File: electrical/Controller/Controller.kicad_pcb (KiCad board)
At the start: 2 copper layers, 30 x 42 mm, 33 parts, among them J1 USB4105-GF-A, J2 SWD_10, J3 TC2030-NL, U1 LP5912-3.3DRV, U2 USBLC6-2P6, U3 STM32L072CBTx, U4 ABPMRRV001PD2A3

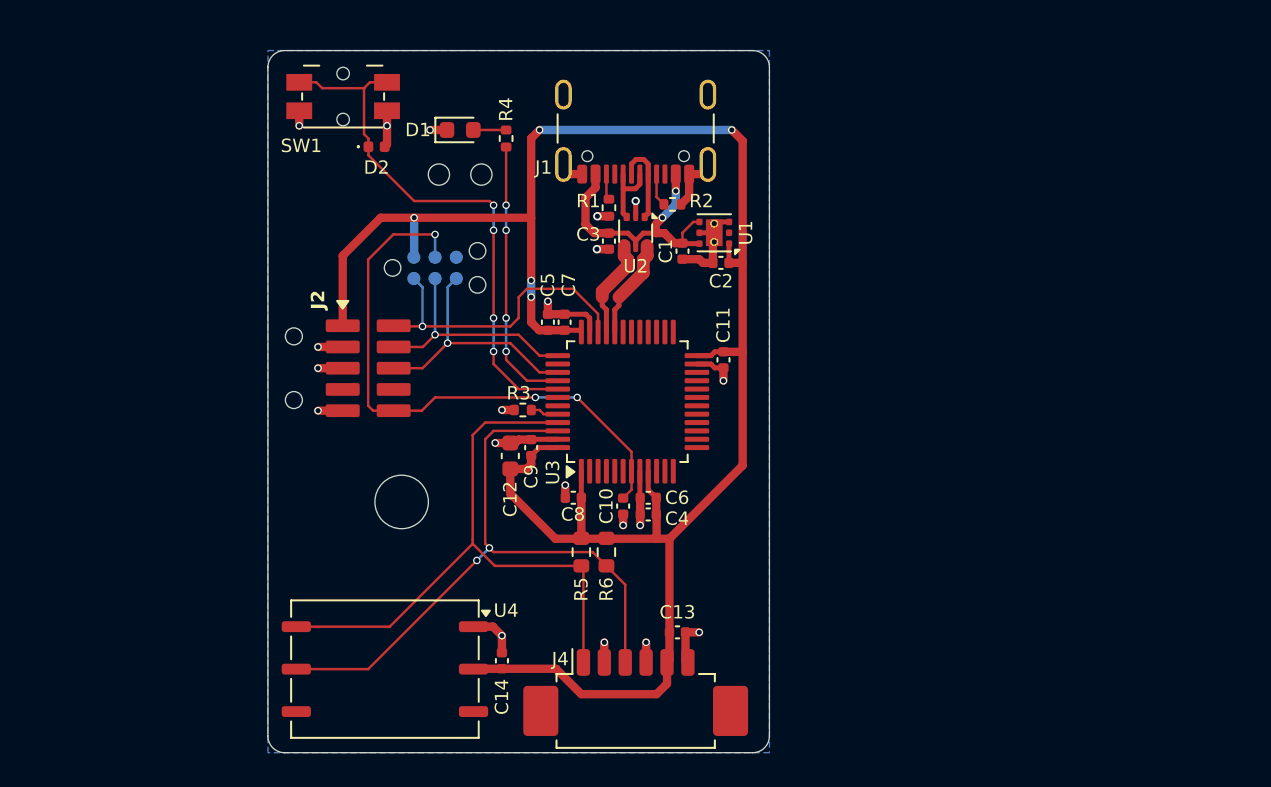
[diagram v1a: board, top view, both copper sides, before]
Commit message: Use wide layout for controller PCB
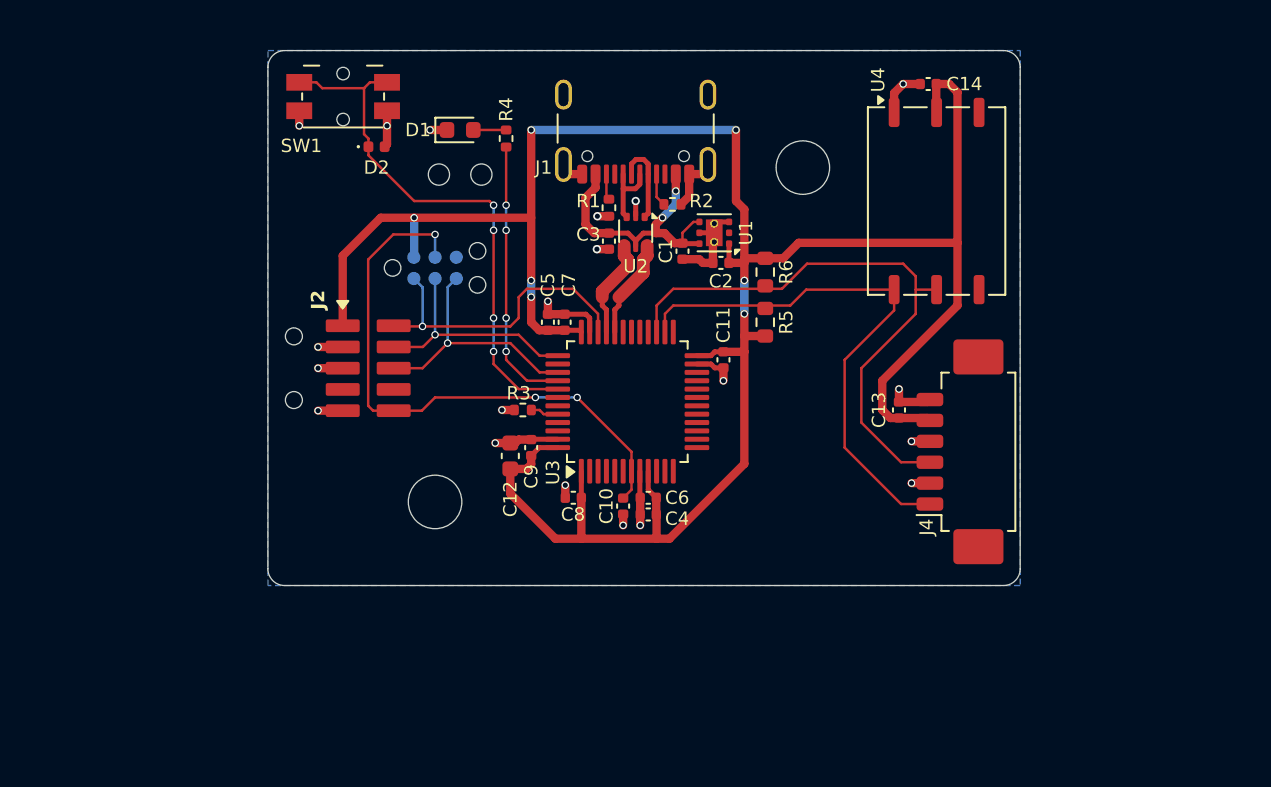
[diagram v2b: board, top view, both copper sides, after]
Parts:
- added H3: MountingHole, MountingHole:MountingHole_3.2mm_M3, F.Cu at (140.0, 97.0)
- moved U4 43.3 mm to (170.0, 79.0), turned to 0 degrees
- moved C14 42.9 mm to (169.5, 72.0), turned to 180 degrees
- moved H2 31.2 mm to (162.0, 77.0)
- moved J4 25.0 mm to (172.0, 94.0), turned to 90 degrees
- moved R6 19.3 mm to (159.8, 83.2)
- moved C13 18.8 mm to (167.8, 91.5), turned to 90 degrees
- moved R5 17.6 mm to (159.8, 86.2), turned to 90 degrees
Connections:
- U3 pad 26: unconnected-(U3-PB13-Pad26) -> /I2C_SCL
- U3 pad 27: unconnected-(U3-PB14-Pad27) -> /I2C_SDA
- U3 pad 45: /I2C_SCL -> unconnected-(U3-PB8-Pad45)
- U3 pad 46: /I2C_SDA -> unconnected-(U3-PB9-Pad46)
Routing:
- net +3.3V: track 121.8 -> 142.9 mm, vias 5 -> 7
- net /I2C_SCL: track 37.4 -> 32.6 mm
- net /I2C_SDA: track 39.4 -> 34.9 mm, vias 2 -> 0
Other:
- board size 30 x 42 mm -> 45 x 32 mm

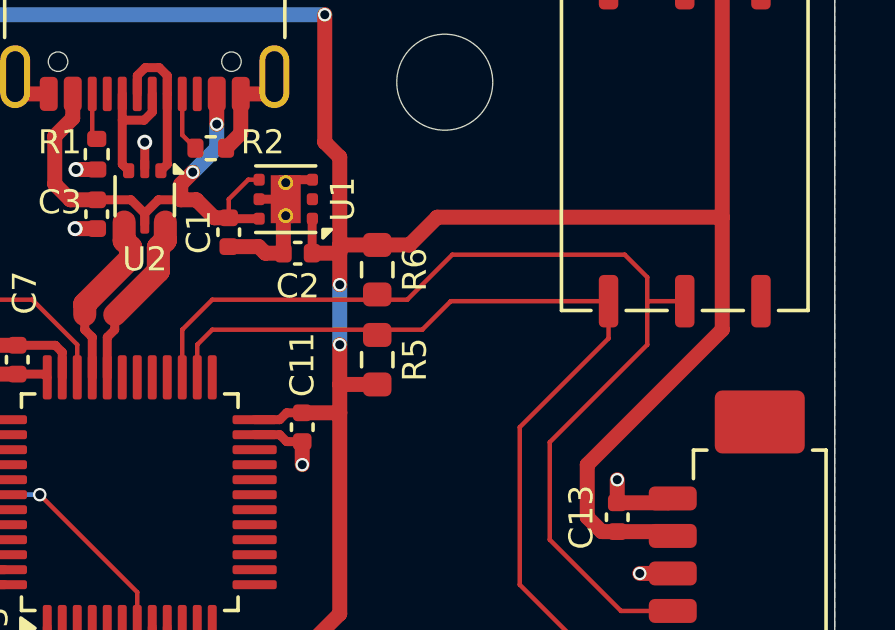
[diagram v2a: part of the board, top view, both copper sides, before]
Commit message: Use 0402 resistors for i2c pull-ups
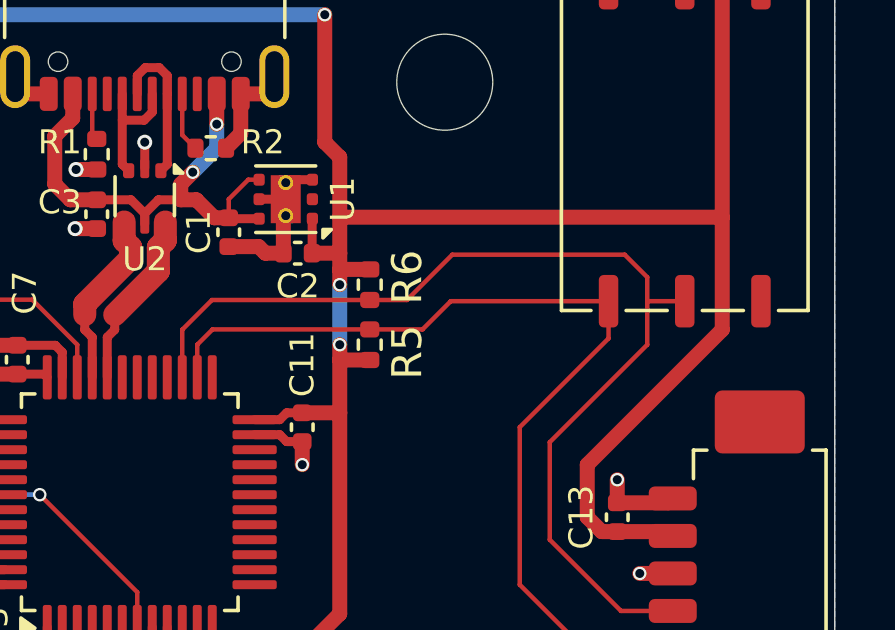
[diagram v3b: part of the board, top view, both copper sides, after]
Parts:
- R5, R6: footprint Resistor_SMD:R_0603_1608Metric -> Resistor_SMD:R_0402_1005Metric
- moved R5 0.56 mm to (159.5, 85.8)
- moved R6 0.56 mm to (159.5, 83.8)
- renumbered H2 to H1, H3 to H2, H1 to H3

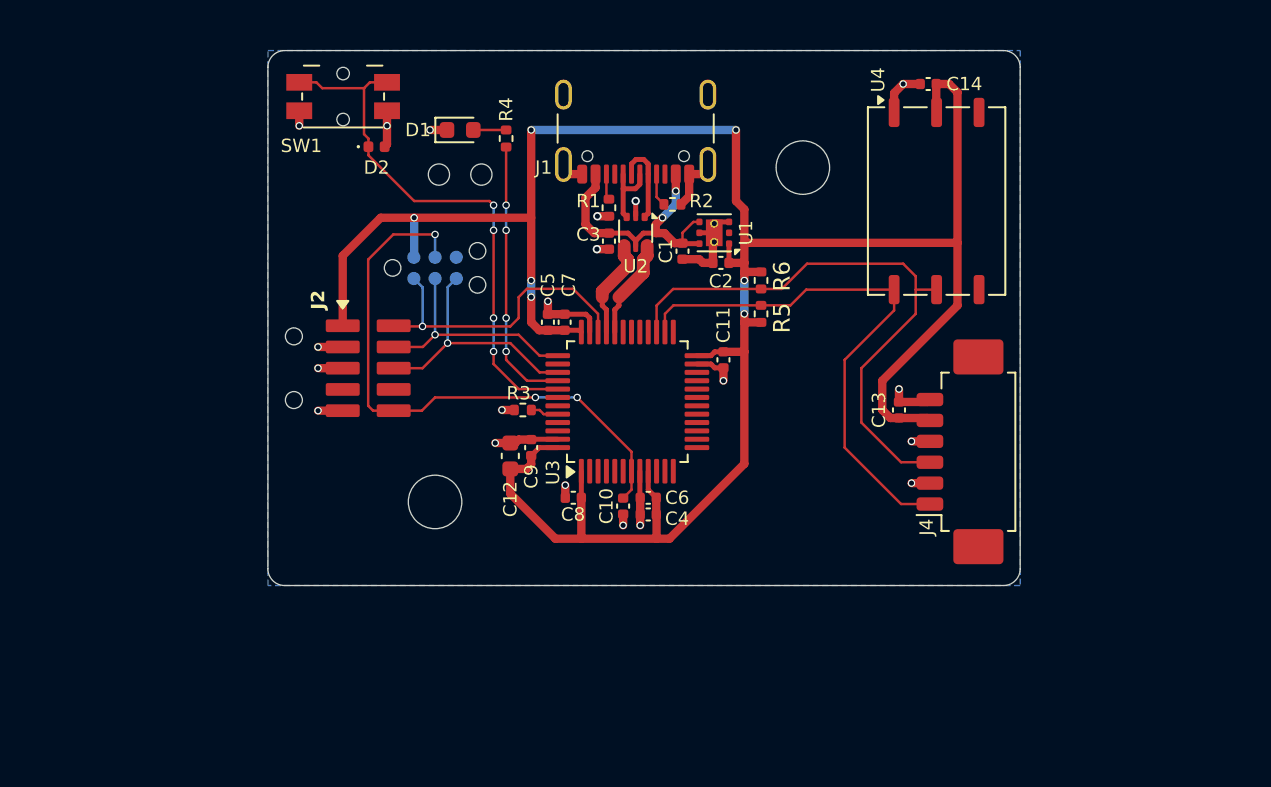
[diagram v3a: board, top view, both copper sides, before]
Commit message: Move debug header within controller bounding rect
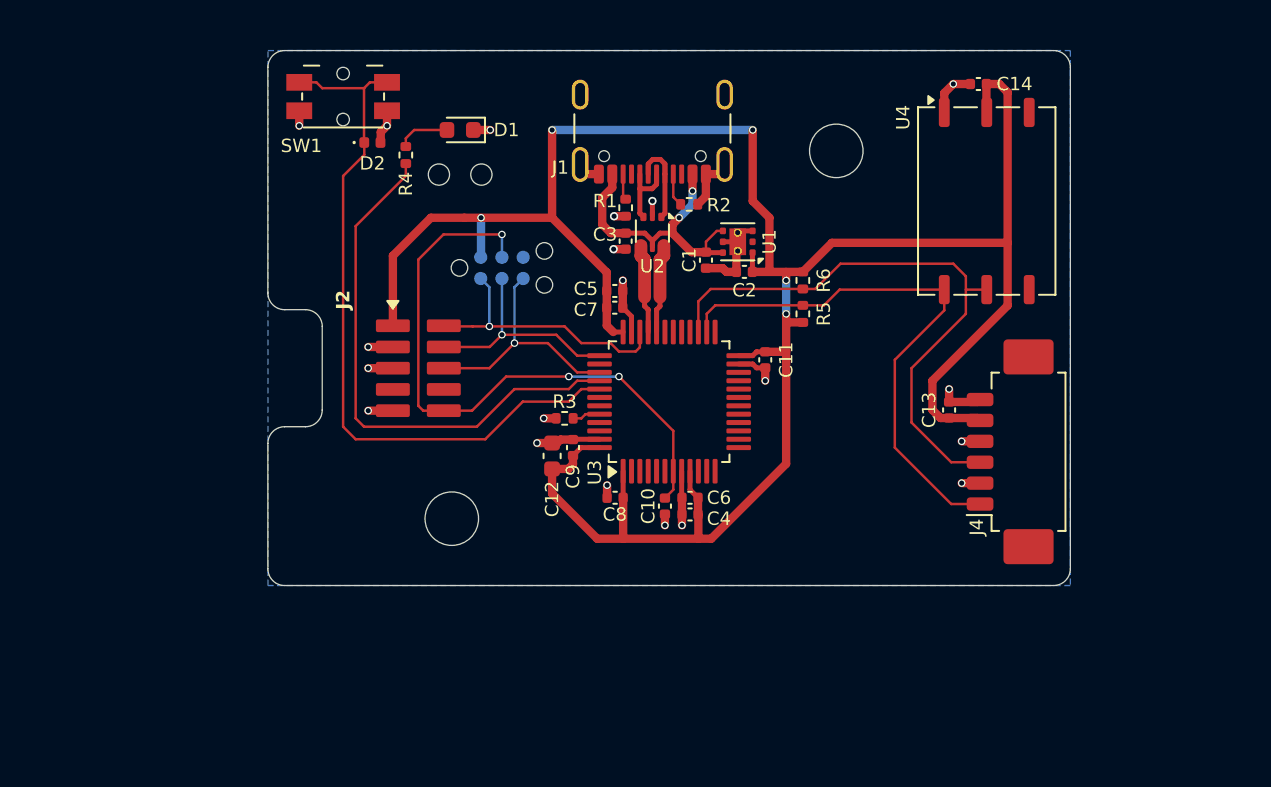
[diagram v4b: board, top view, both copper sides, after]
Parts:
- moved R4 6.08 mm to (138.2, 76.2)
- moved C5 4.42 mm to (150.8, 84.4), turned to 0 degrees
- moved J3 4.00 mm to (144.0, 83.0)
- moved C7 3.12 mm to (150.8, 85.4), turned to 0 degrees
- moved C13 3.00 mm to (170.8, 91.5)
- moved C14 3.00 mm to (172.5, 72.0)
- moved J2 3.00 mm to (139.0, 89.0)
- moved J4 3.00 mm to (175.0, 94.0)
- moved U4 3.00 mm to (173.0, 79.0)
- moved R3 2.55 mm to (147.8, 92.0)
- moved C10 2.50 mm to (153.8, 97.2)
- moved C11 2.50 mm to (159.8, 88.5)
- moved C12 2.50 mm to (147.0, 94.2)
- moved C4 2.50 mm to (155.2, 97.8)
- moved C6 2.50 mm to (155.2, 96.8)
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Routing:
- net Net-(U3-PB4): track 16.3 -> 32.4 mm, vias 4 -> 0
- net Net-(D2-K): track 32.3 -> 43.2 mm, vias 4 -> 0
- net NRST: track 35.3 -> 37.5 mm
- net /SWDIO: track 18.7 -> 16.5 mm
- net Net-(D1-A): track 1.96 -> 3.16 mm
- net GND: track 44.7 -> 43.7 mm
- net +3.3V: track 143.3 -> 142.3 mm, vias 7 -> 5
- net /USB_D+: track 6.01 -> 5.36 mm
- net /I2C_SDA: track 34.9 -> 35.5 mm
- net /USB_D-: track 5.98 -> 5.36 mm
- net VBUS: track 17.2 -> 17.8 mm
- net /SWCLK: track 14.0 -> 13.5 mm
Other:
- board size 45 x 32 mm -> 48 x 32 mm

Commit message: Change controller board form factor
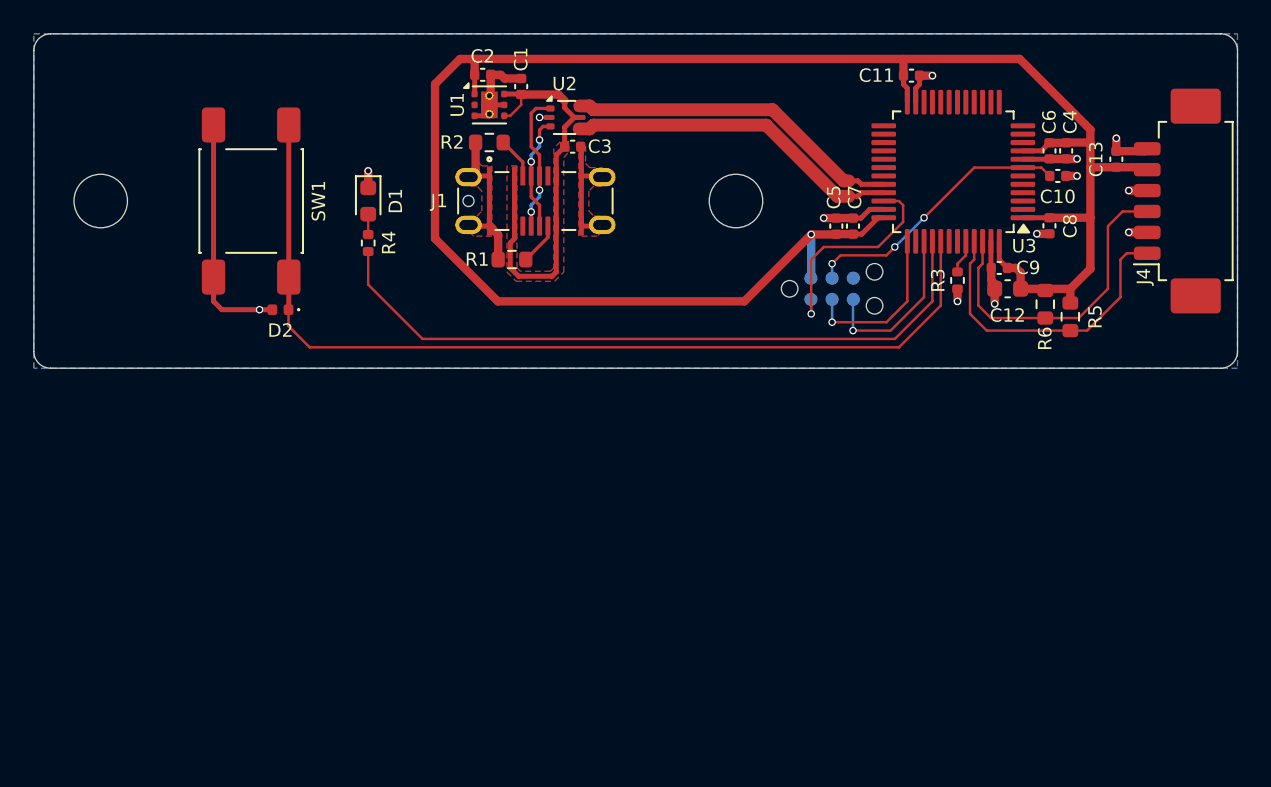
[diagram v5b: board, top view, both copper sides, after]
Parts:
- removed C14: 100n, Capacitor_SMD:C_0402_1005Metric
- removed H3: SLP3-150-150-F, MidiConcertina:Bivar_SLP3-150-150-F
- removed J2: SWD_10, MidiConcertina:Samtech_FTSH-105-01-L-DH
- removed U4: ABPMRRV001PD2A3, MidiConcertina:Honeywell_ABPMRRx
- J1: value USB4105-GF-A -> USB4145-03-0170-C; footprint Connector_USB:USB_C_Receptacle_GCT_USB4105-xx-A_16P_TopMnt_Horizontal -> MidiConcertina:USB_C_Receptacle_GCT-USB4145
- R1, R2, R5, R6: footprint Resistor_SMD:R_0402_1005Metric -> Resistor_SMD:R_0603_1608Metric
- SW1: footprint Button_Switch_SMD:Panasonic_EVQPUL_EVQPUC -> Button_Switch_SMD:SW_Push_1P1T_NO_E-Switch_TL3301NxxxxxG
- moved C4 31.3 mm to (177.8, 76.0), turned to -90 degrees
- moved C10 30.7 mm to (177.2, 77.5), turned to 0 degrees
- moved C8 30.7 mm to (176.8, 80.5), turned to -90 degrees
- moved C6 29.9 mm to (176.8, 76.0), turned to -90 degrees
- moved C12 29.0 mm to (174.2, 84.2), turned to 180 degrees
- moved H2 28.3 mm to (120.0, 79.0)
- moved C9 27.7 mm to (173.8, 83.0), turned to 180 degrees
- moved R3 24.9 mm to (171.2, 83.8), turned to -90 degrees
- moved U3 21.9 mm to (171.0, 77.2), turned to 180 degrees
- moved J3 19.8 mm to (163.8, 84.2)
- moved C2 19.6 mm to (142.8, 71.5), turned to 0 degrees
- moved C11 19.1 mm to (168.5, 71.5), turned to 0 degrees
- moved C13 18.0 mm to (180.8, 76.5)
- moved J4 18.0 mm to (185.0, 79.0)
- moved U1 17.0 mm to (143.2, 73.2), turned to 0 degrees
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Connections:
- U3 pad 26: /I2C_SCL -> unconnected-(U3-PB13-Pad26)
- U3 pad 27: /I2C_SDA -> unconnected-(U3-PB14-Pad27)
- U3 pad 45: unconnected-(U3-PB8-Pad45) -> /I2C_SCL
- U3 pad 46: unconnected-(U3-PB9-Pad46) -> /I2C_SDA
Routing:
- net +3.3V: track 142.3 -> 118.1 mm, vias 5 -> 1
- net NRST: track 37.5 -> 16.5 mm
- net /I2C_SDA: track 35.5 -> 19.2 mm
- net /USB_D+: track 5.36 -> 20.2 mm
- net /USB_D-: track 5.36 -> 20.1 mm
- net GND: track 43.7 -> 58.3 mm, vias 20 -> 13
- net /I2C_SCL: track 33.1 -> 18.7 mm
- net Net-(D2-K): track 43.2 -> 56.5 mm
- net Net-(U3-PB4): track 32.4 -> 41.6 mm
- net VBUS: track 17.8 -> 25.6 mm, vias 2 -> 0
- net UART_TX: track 14.7 -> 10.3 mm
- net /SWDIO: track 16.5 -> 12.8 mm
- net /SWCLK: track 13.5 -> 9.97 mm
- net Net-(J1-D--PadA7): track 5.09 -> 8.43 mm, vias 0 -> 2
- net Net-(J1-D+-PadA6): track 4.37 -> 6.90 mm, vias 0 -> 2
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- added copper zone on F.Cu, net GND
- added copper zone on F.Cu, net VBUS
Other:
- board size 48 x 32 mm -> 72 x 20 mm
- board text removed: "Enclosure Exterior"
